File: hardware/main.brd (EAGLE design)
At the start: 123.2 x 61.9 mm, 12 parts, among them X1 22-23-2021

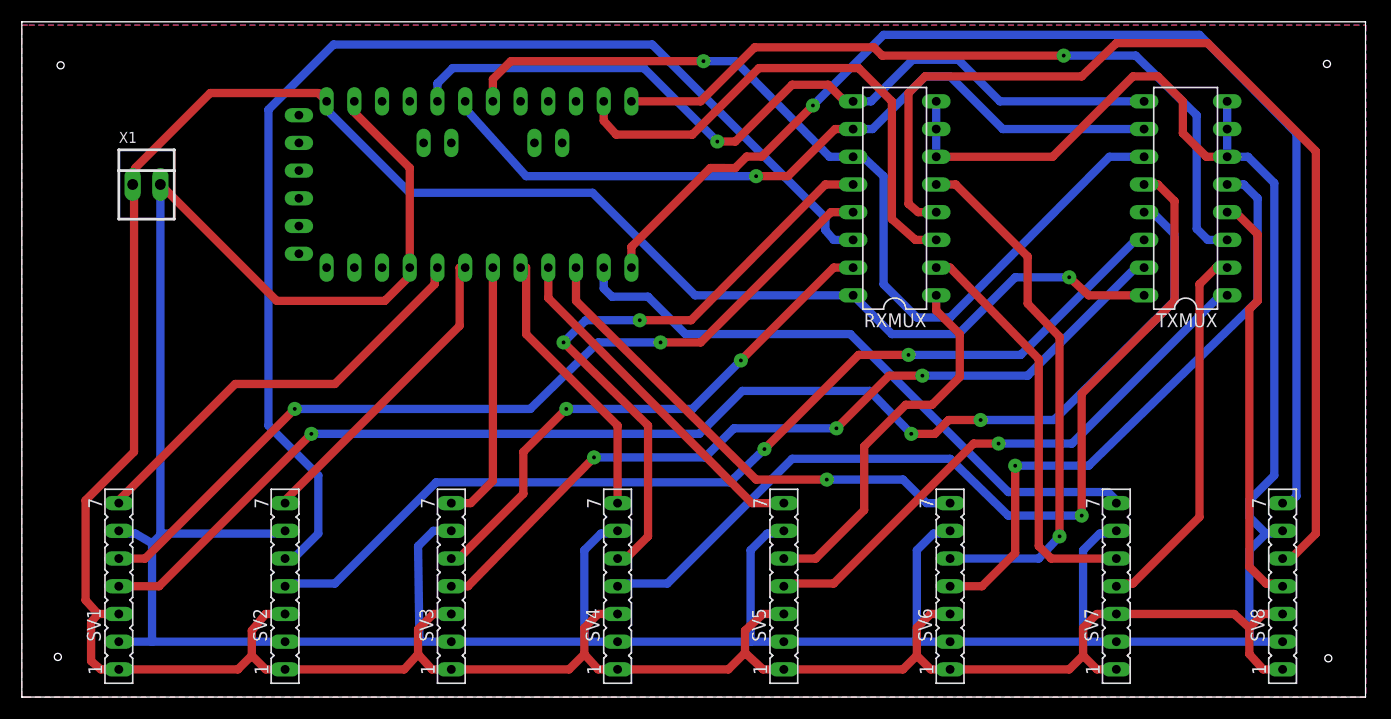
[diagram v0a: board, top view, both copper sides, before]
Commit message: adding ATX control electronics
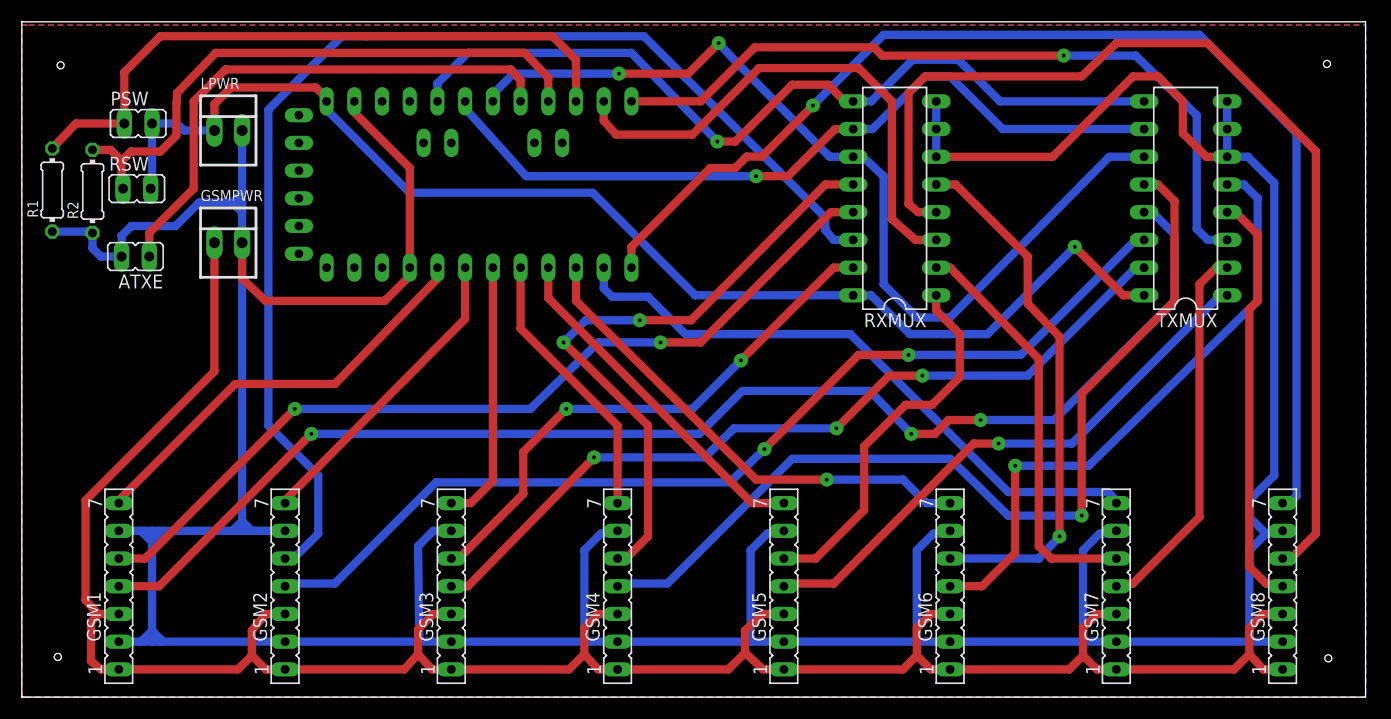
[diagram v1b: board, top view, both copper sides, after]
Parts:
- removed X1: 22-23-2021, con-molex:22-23-2021
- added ATXE: EN, jumper:JP1
- added GSMPWR, LPWR: VCC GND, con-molex:22-23-2021
- added PSW, RSW: (no value), jumper:JP1
- added R1, R2: 10K, eagle-ltspice:0204/7
- ARDUINO: value PRO-MINI-2 -> PRO-MINI
- GSM1, GSM2, GSM3, GSM4, GSM5, GSM6, GSM7, GSM8: value (none) -> SIM800L
- renumbered SV1 to GSM1, SV2 to GSM2, SV3 to GSM3, SV4 to GSM4, SV5 to GSM5, SV6 to GSM6, SV7 to GSM7, SV8 to GSM8, U$1 to ARDUINO
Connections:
- new net N$5: ARDUINO.D13, R2.2, RSW.1
- new net N$7: ARDUINO.A3, ATXE.1
- new net N$9: ARDUINO.D12, PSW.1, R1.2
- new net VDD: GSM1.1, GSM1.3, GSM2.1, GSM2.3, GSM3.1, GSM3.3, GSM4.1, GSM4.3, GSM5.1, GSM5.3, GSM6.1, GSM6.3, GSM7.1, GSM7.3, GSM8.1, GSM8.3, GSMPWR.1
- net GND: now also ATXE.2, GSMPWR.2, LPWR.2, R1.1, R2.1; no longer X1.2
- net VCC: now also LPWR.1, PSW.2, RSW.2; no longer GSM1.1, GSM1.3, GSM2.1, GSM2.3, GSM3.1, GSM3.3, GSM4.1, GSM4.3, GSM5.1, GSM5.3, GSM6.1, GSM6.3, GSM7.1, GSM7.3, GSM8.1, GSM8.3, X1.1
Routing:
- net VDD: track 0.00 -> 205.9 mm
- net VCC: track 317.6 -> 116.4 mm
- net N$9: track 0.00 -> 59.8 mm
- net N$5: track 0.00 -> 54.3 mm
- net N$7: track 0.00 -> 49.5 mm
- net GND: track 368.3 -> 397.3 mm
- net ADDR2: track 75.7 -> 77.0 mm
- net RX1: track 108.9 -> 109.6 mm
- net ADDR0: track 84.1 -> 84.7 mm, vias 1 -> 2

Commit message: adding extra power supply for GSM, and connecting to gsm power through a jumper
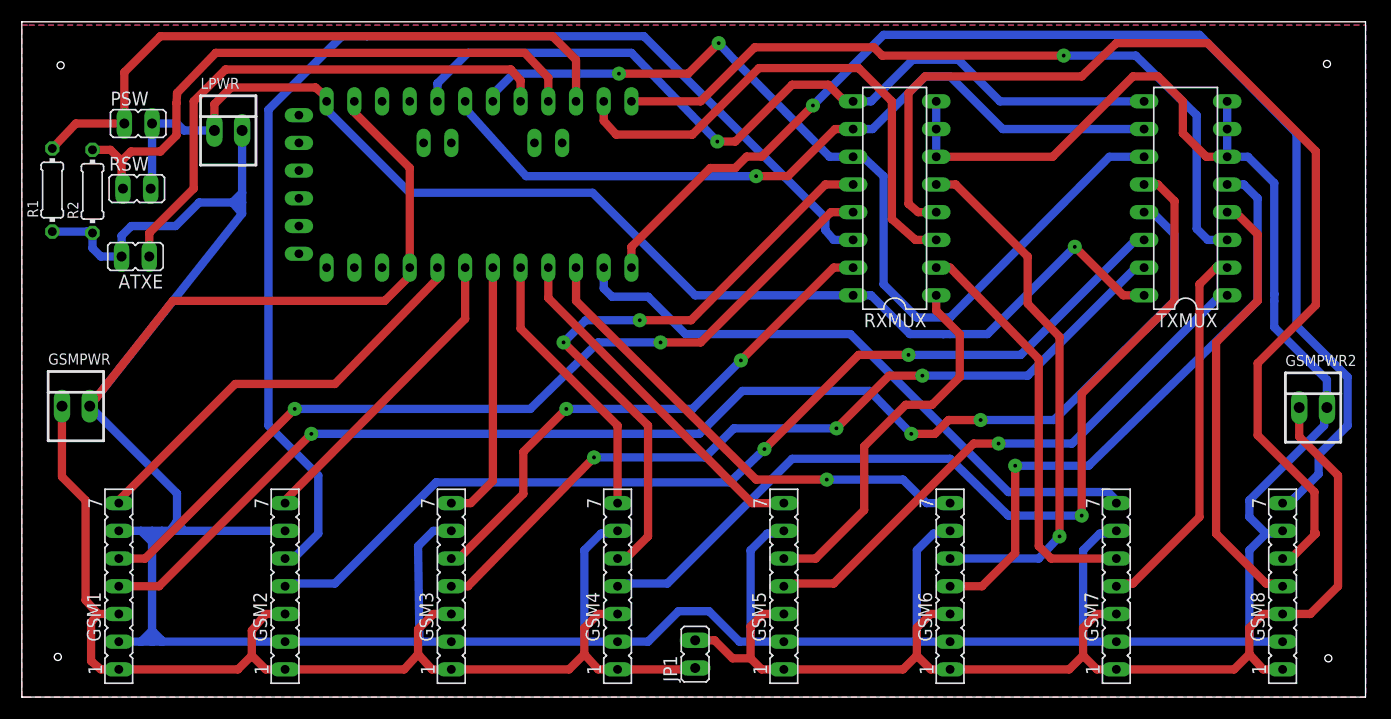
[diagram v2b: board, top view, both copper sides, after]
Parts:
- added GSMPWR2: VCC GND, con-molex:22-23-2021
- added JP1: (no value), jumper:JP1
- moved GSMPWR 20.5 mm to (45.6, 25.4)
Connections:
- new net N$6: GSM5.1, GSM5.3, GSM6.1, GSM6.3, GSM7.1, GSM7.3, GSM8.1, GSM8.3, GSMPWR2.1, JP1.2
- net GND: now also GSMPWR2.2
- net VDD: now also JP1.1; no longer GSM5.1, GSM5.3, GSM6.1, GSM6.3, GSM7.1, GSM7.3, GSM8.1, GSM8.3
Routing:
- net N$6: track 0.00 -> 107.4 mm
- net VDD: track 205.9 -> 104.1 mm
- net GND: track 397.3 -> 426.0 mm
- net RX7: track 95.3 -> 99.7 mm
- net ENABLE7: track 109.5 -> 113.3 mm
- net TX7: track 38.5 -> 41.1 mm
